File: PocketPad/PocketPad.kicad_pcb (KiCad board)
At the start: 2 copper layers, 72.6 x 62.7 mm, 39 parts, among them SW0 SW_Push, SW1 SW_Push, SW10 SW_Push, SW11 SW_Push, SW12 SW_Push, SW13 SW_Push, SW14 SW_Push, SW15 SW_Push, SW16 SW_Push, SW17 SW_Push, SW18 SW_Push, SW2 SW_Push, SW3 SW_Push, SW4 SW_Push, SW5 SW_Push, SW6 SW_Push, SW7 SW_Push, SW8 SW_Push, SW9 SW_Push

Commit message: Mounting Holes
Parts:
- added REF**: MountingHole_2.2mm_M2, MountingHole:MountingHole_2.2mm_M2, F.Cu at (25.7, 96.3)
- added REF**: MountingHole_2.2mm_M2, MountingHole:MountingHole_2.2mm_M2, F.Cu at (94.7, 36.8)
- added REF**: MountingHole_2.2mm_M2, MountingHole:MountingHole_2.2mm_M2, F.Cu at (25.7, 36.8)
- added REF**: MountingHole_2.2mm_M2, MountingHole:MountingHole_2.2mm_M2, F.Cu at (94.7, 96.3)
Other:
- board size 72.6 x 62.7 mm -> 71.6 x 62 mm
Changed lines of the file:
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@@
     )
+  )
+  (footprint "MountingHole:MountingHole_2.2mm_M2" (layer "F.Cu")
+    (at 25.654 96.266)
+    (descr "Mounting Hole 2.2mm, no annular, M2")
+    (tags "mounting hole 2.2mm no annular m2")
+    (attr exclude_from_pos_files exclude_from_bom)
+    (fp_text reference "REF**" (at 0 -3.2) (layer "F.SilkS") hide
+      (effects (font (size 1 1) (thickness 0.15)))
+    )
+    (fp_text value "MountingHole_2.2mm_M2" (at 0 3.2) (layer "F.Fab") hide
+      (effects (font (size 1 1) (thickness 0.15)))
+    )
+    (fp_text user "${REFERENCE}" (at 0 0) (layer "F.Fab") hide
+      (effects (font (size 1 1) (thickness 0.15)))
+    )
+    (fp_circle (center 0 0) (end 2.2 0) (layer "Cmts.User") (width 0.15) (fill none))
+    (fp_circle (center 0 0) (end 2.45 0) (layer "F.CrtYd") (width 0.05) (fill none))
+    (pad "" np_thru_hole circle (at 0 0) (size 2.2 2.2) (drill 2.2) (layers *.Cu *.Mask))
+  )
+  (footprint "MountingHole:MountingHole_2.2mm_M2" (layer "F.Cu")
+    (at 94.742 36.83)
+    (descr "Mounting Hole 2.2mm, no annular, M2")
+    (tags "mounting hole 2.2mm no annular m2")
+    (attr exclude_from_pos_files exclude_from_bom)
+    (fp_text reference "REF**" (at 0 -3.2) (layer "F.SilkS") hide
+      (effects (font (size 1 1) (thickness 0.15)))
+    )
+    (fp_text value "MountingHole_2.2mm_M2" (at 0 3.2) (layer "F.Fab") hide
+      (effects (font (size 1 1) (thickness 0.15)))
+    )
+    (fp_text user "${REFERENCE}" (at 0 0) (layer "F.Fab") hide
+      (effects (font (size 1 1) (thickness 0.15)))
+    )
+    (fp_circle (center 0 0) (end 2.2 0) (layer "Cmts.User") (width 0.15) (fill none))
+    (fp_circle (center 0 0) (end 2.45 0) (layer "F.CrtYd") (width 0.05) (fill none))
+    (pad "" np_thru_hole circle (at 0 0) (size 2.2 2.2) (drill 2.2) (layers F&B.Cu *.Mask))
   )
   (footprint "Keebio:Switch_6x6x8.5" (layer "F.Cu")
@@
     )
   )
+  (footprint "MountingHole:MountingHole_2.2mm_M2" (layer "F.Cu")
+    (at 25.654 36.83)
+    (descr "Mounting Hole 2.2mm, no annular, M2")
+    (tags "mounting hole 2.2mm no annular m2")
+    (attr exclude_from_pos_files exclude_from_bom)
+    (fp_text reference "REF**" (at 0 -3.2) (layer "F.SilkS") hide
+      (effects (font (size 1 1) (thickness 0.15)))
+    )
+    (fp_text value "MountingHole_2.2mm_M2" (at 0 3.2) (layer "F.Fab") hide
+      (effects (font (size 1 1) (thickness 0.15)))
+    )
+    (fp_text user "${REFERENCE}" (at 0 0) (layer "F.Fab") hide
+      (effects (font (size 1 1) (thickness 0.15)))
+    )
+    (fp_circle (center 0 0) (end 2.2 0) (layer "Cmts.User") (width 0.15) (fill none))
+    (fp_circle (center 0 0) (end 2.45 0) (layer "F.CrtYd") (width 0.05) (fill none))
+    (pad "" np_thru_hole circle (at 0 0) (size 2.2 2.2) (drill 2.2) (layers F&B.Cu *.Mask))
+  )
   (footprint "Diode_THT:D_DO-35_SOD27_P7.62mm_Horizontal" (layer "F.Cu")
     (at 84.582 50.038 90)
@@
     )
   )
+  (footprint "MountingHole:MountingHole_2.2mm_M2" (layer "F.Cu")
+    (at 94.742 96.266)
+    (descr "Mounting Hole 2.2mm, no annular, M2")
+    (tags "mounting hole 2.2mm no annular m2")
+    (attr exclude_from_pos_files exclude_from_bom)
+    (fp_text reference "REF**" (at 0 -3.2) (layer "F.SilkS") hide
+      (effects (font (size 1 1) (thickness 0.15)))
+    )
+    (fp_text value "MountingHole_2.2mm_M2" (at 0 3.2) (layer "F.Fab") hide
+      (effects (font (size 1 1) (thickness 0.15)))
+    )
+    (fp_text user "${REFERENCE}" (at 0 0) (layer "F.Fab") hide
+      (effects (font (size 1 1) (thickness 0.15)))
+    )
+    (fp_circle (center 0 0) (end 2.2 0) (layer "Cmts.User") (width 0.15) (fill none))
+    (fp_circle (center 0 0) (end 2.45 0) (layer "F.CrtYd") (width 0.05) (fill none))
+    (pad "" np_thru_hole circle (at 0 0) (size 2.2 2.2) (drill 2.2) (layers *.Cu *.Mask))
+  )
   (footprint "Keebio:Switch_6x6x8.5" (layer "F.Cu")
     (at 76.454 64.516)
@@
     )
   )
-  (gr_circle (center 94.8 96.3) (end 95.95 96.3) (layer "Edge.Cuts") (width 0.2) (fill none))
-  (gr_circle (center 25.6 96.3) (end 26.75 96.3) (layer "Edge.Cuts") (width 0.2) (fill none))
-  (gr_rect (start 23.876 35.306) (end 96.52 98.044) (layer "Edge.Cuts") (width 0.1) (fill none))
-  (gr_circle (center 25.6 37) (end 26.75 37) (layer "Edge.Cuts") (width 0.2) (fill none))
-  (gr_circle (center 94.8 37) (end 95.95 37) (layer "Edge.Cuts") (width 0.2) (fill none))
+  (gr_rect (start 24.384 35.56) (end 96.012 97.536) (layer "Edge.Cuts") (width 0.1) (fill none))
   (segment (start 49.022 87.884) (end 49.022 90.088) (width 0.25) (layer "F.Cu") (net 3))
   (segment (start 49.022 90.088) (end 48.954 90.156) (width 0.25) (layer "F.Cu") (net 3))

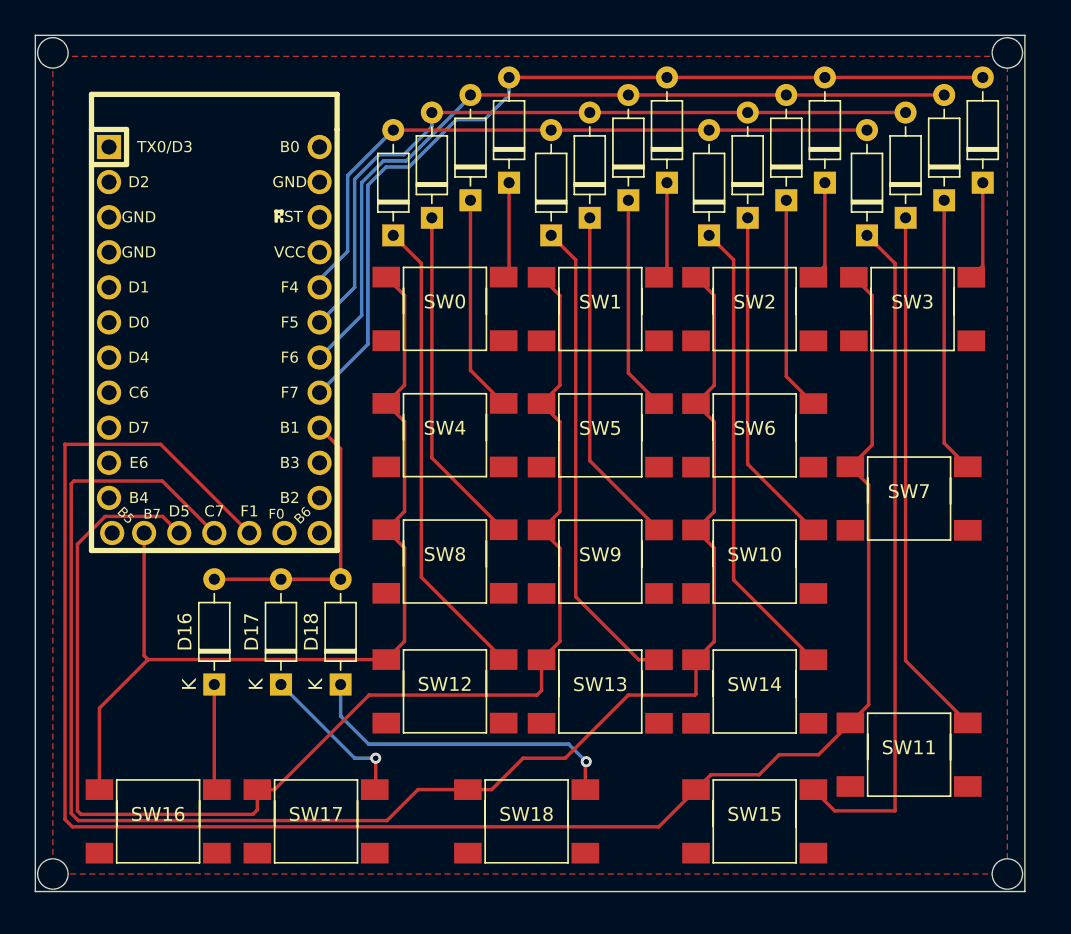
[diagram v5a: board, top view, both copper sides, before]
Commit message: Edgecut expanded
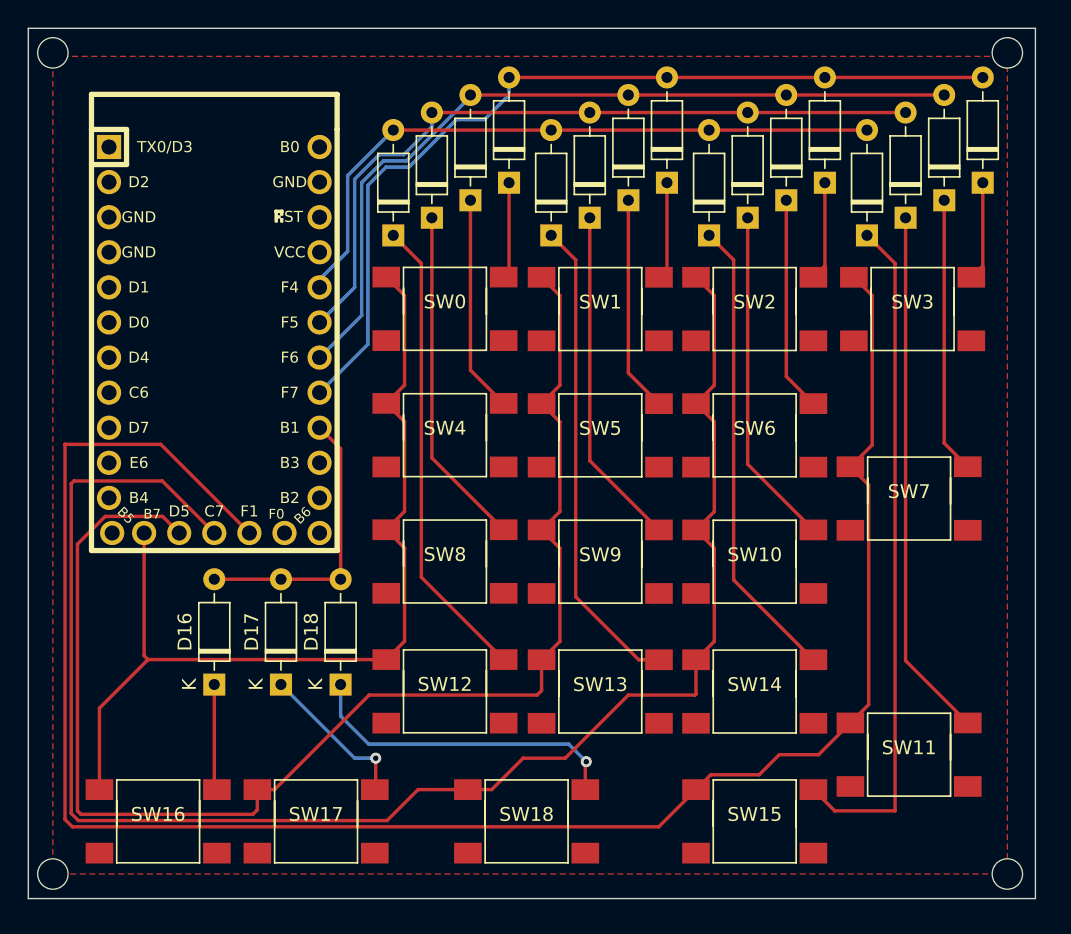
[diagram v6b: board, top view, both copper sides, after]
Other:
- board size 71.6 x 62 mm -> 72.9 x 63 mm
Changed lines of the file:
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@@
     )
   )
-  (gr_rect (start 24.384 35.56) (end 96.012 97.536) (layer "Edge.Cuts") (width 0.1) (fill none))
+  (gr_rect (start 23.876 35.052) (end 96.774 98.044) (layer "Edge.Cuts") (width 0.1) (fill none))
   (segment (start 49.022 87.884) (end 49.022 90.088) (width 0.25) (layer "F.Cu") (net 3))
   (segment (start 49.022 90.088) (end 48.954 90.156) (width 0.25) (layer "F.Cu") (net 3))
